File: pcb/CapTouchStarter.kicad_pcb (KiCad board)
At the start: 4 copper layers, 76.5 x 66 mm, 59 parts, among them J1 USB_C_Receptacle, J2 62684-50110, J3 Conn_ARM_JTAG_SWD_10, Q1 SS8050-G, Q2 SS8050-G, SW1 BOOT, SW2 EN, SW3 SW_SPDT, U1 CP2102N-A01-GQFN28, U2 1965-ESP32-WROOM-32E(8MB)CT-ND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

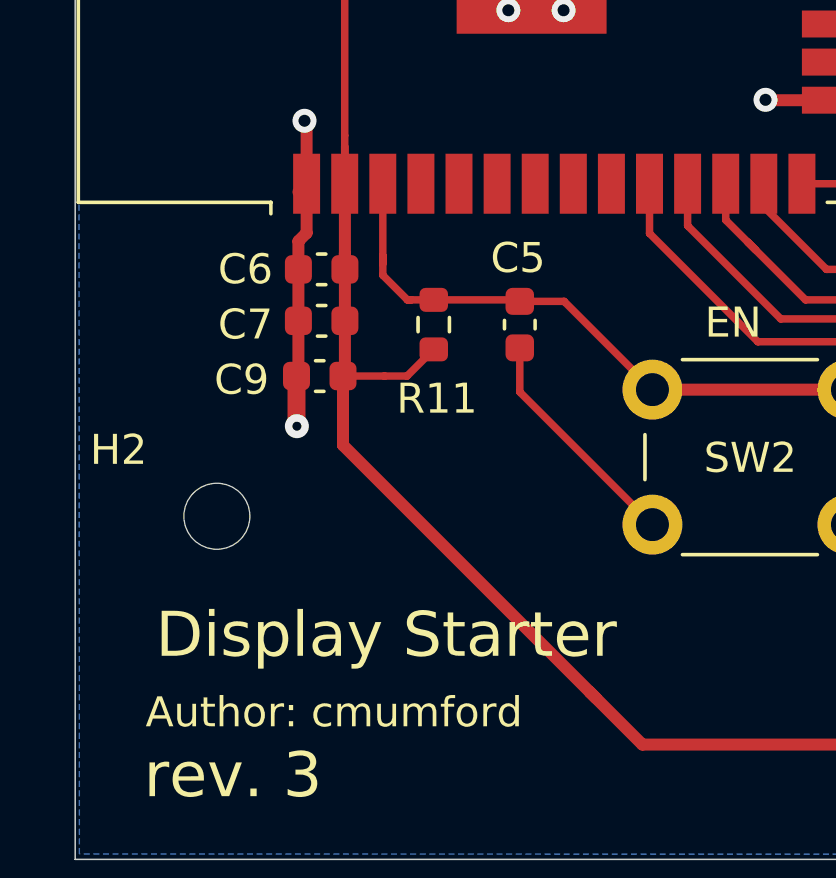
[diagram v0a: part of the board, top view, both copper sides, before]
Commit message: Add a voltage detector.
Add a BD48K33G-TLCT-ND voltage detector.
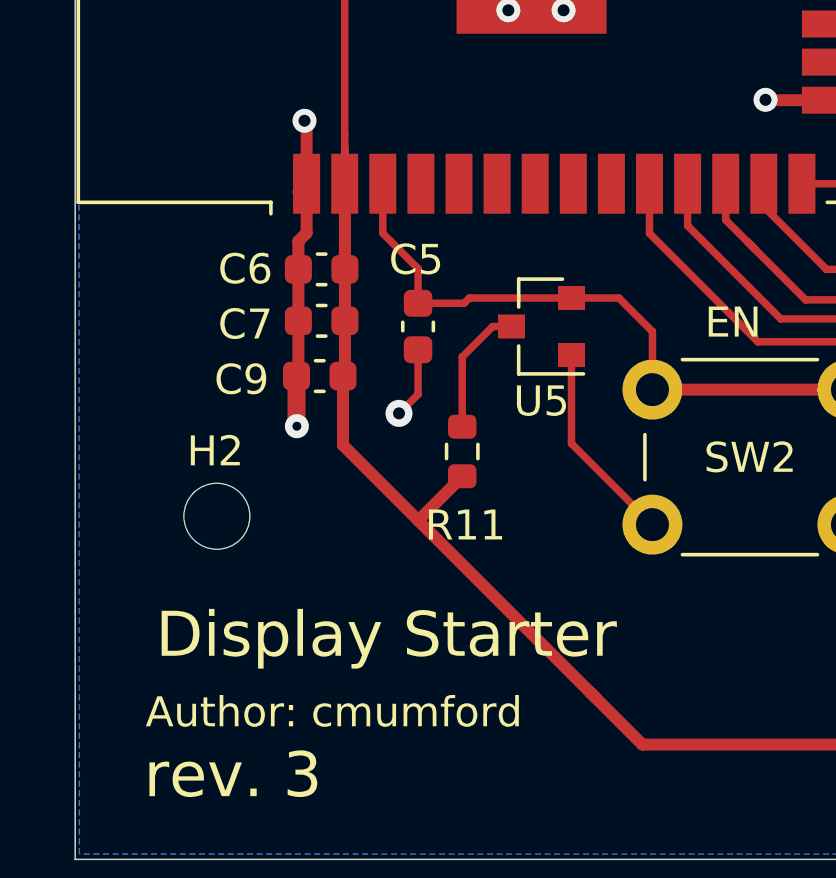
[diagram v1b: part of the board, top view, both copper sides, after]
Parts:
- added U5: BD48K33G-TLCT-ND, Package_TO_SOT_SMD:SOT-23, F.Cu at (144.0, 126.2)
- moved R11 4.33 mm to (141.4, 130.4)
- moved C5 3.39 mm to (139.9, 126.2)
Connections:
- R11 pad 2: EN -> Net-(R11-Pad2)
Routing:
- net Net-(R11-Pad2): track 0.00 -> 4.39 mm
- net GND: track 94.9 -> 96.3 mm, vias 39 -> 40
- net +3V3: track 305.0 -> 303.7 mm
- net EN: track 50.1 -> 50.9 mm

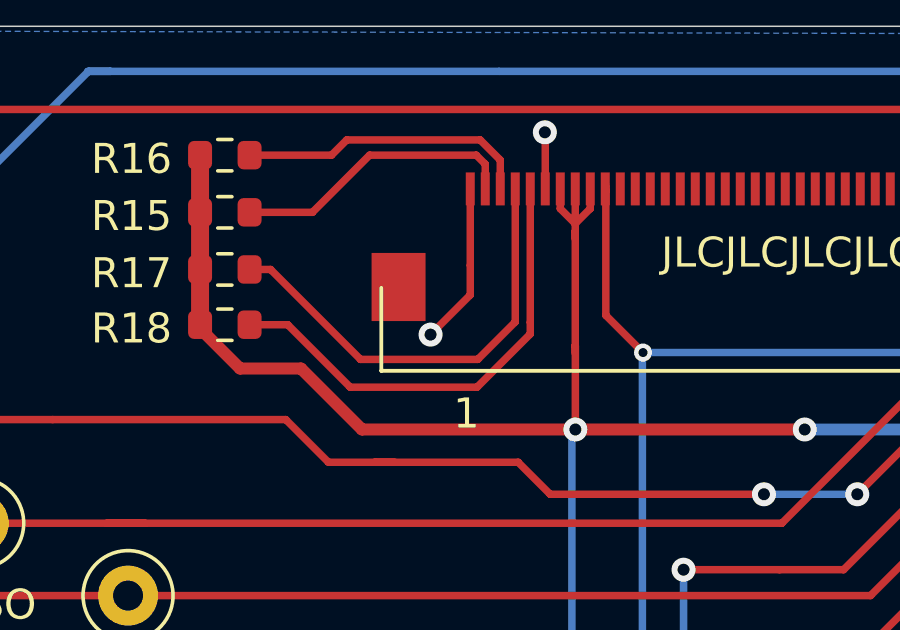
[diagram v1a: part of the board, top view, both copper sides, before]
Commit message: Fixed ground via overlapping display anchor pad.
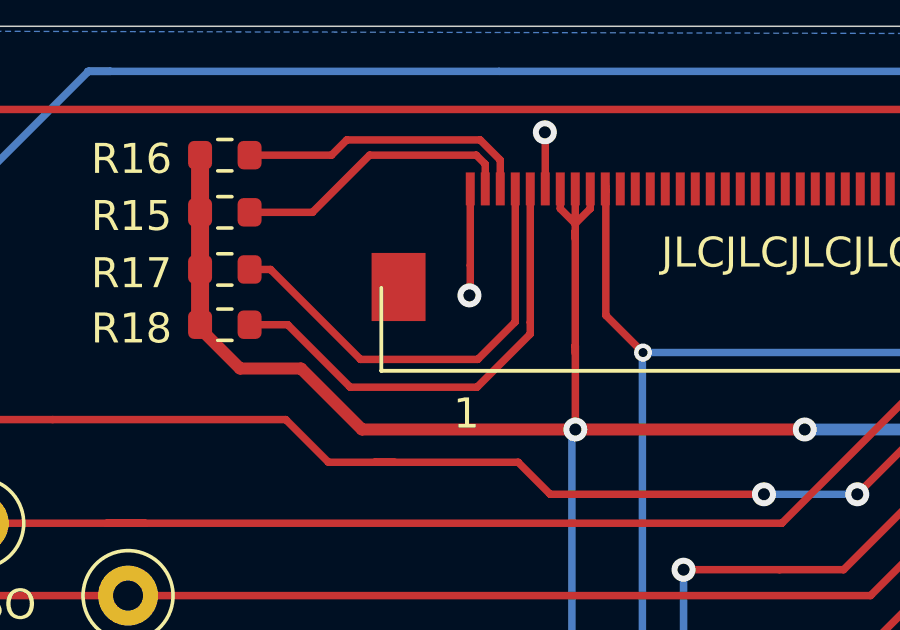
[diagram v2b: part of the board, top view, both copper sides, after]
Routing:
- net GND: track 96.3 -> 94.4 mm

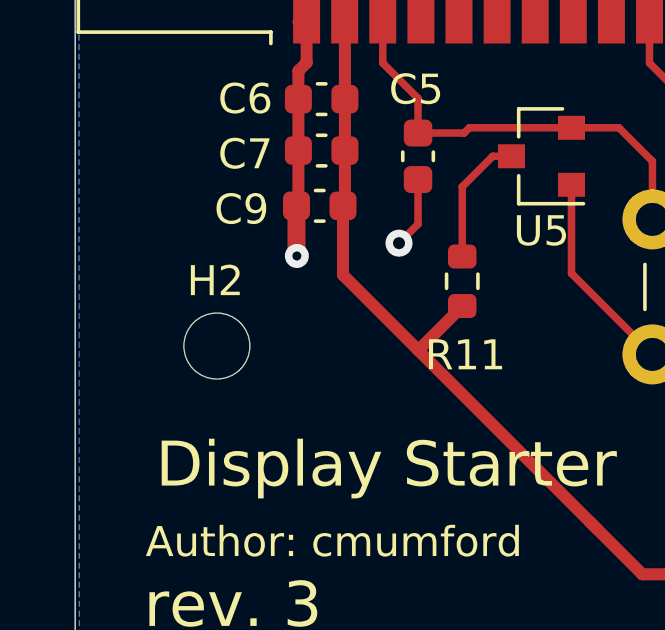
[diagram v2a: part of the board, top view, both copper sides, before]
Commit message: Added antenna keep-out zone for copper fill.
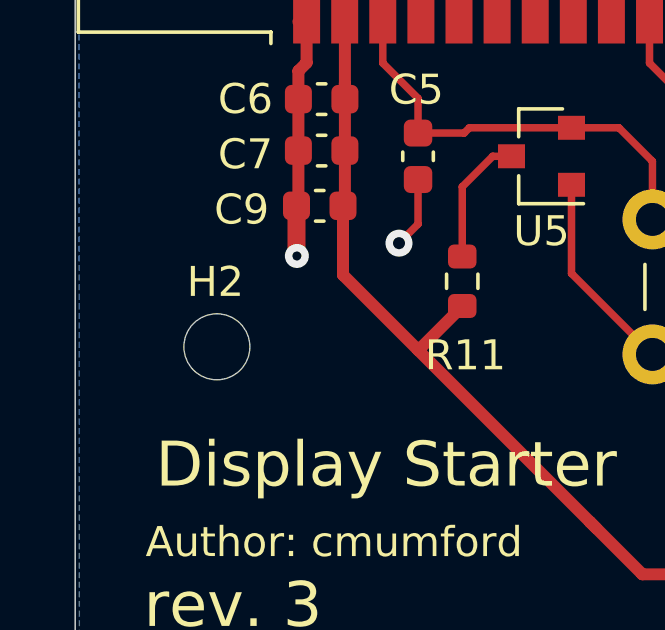
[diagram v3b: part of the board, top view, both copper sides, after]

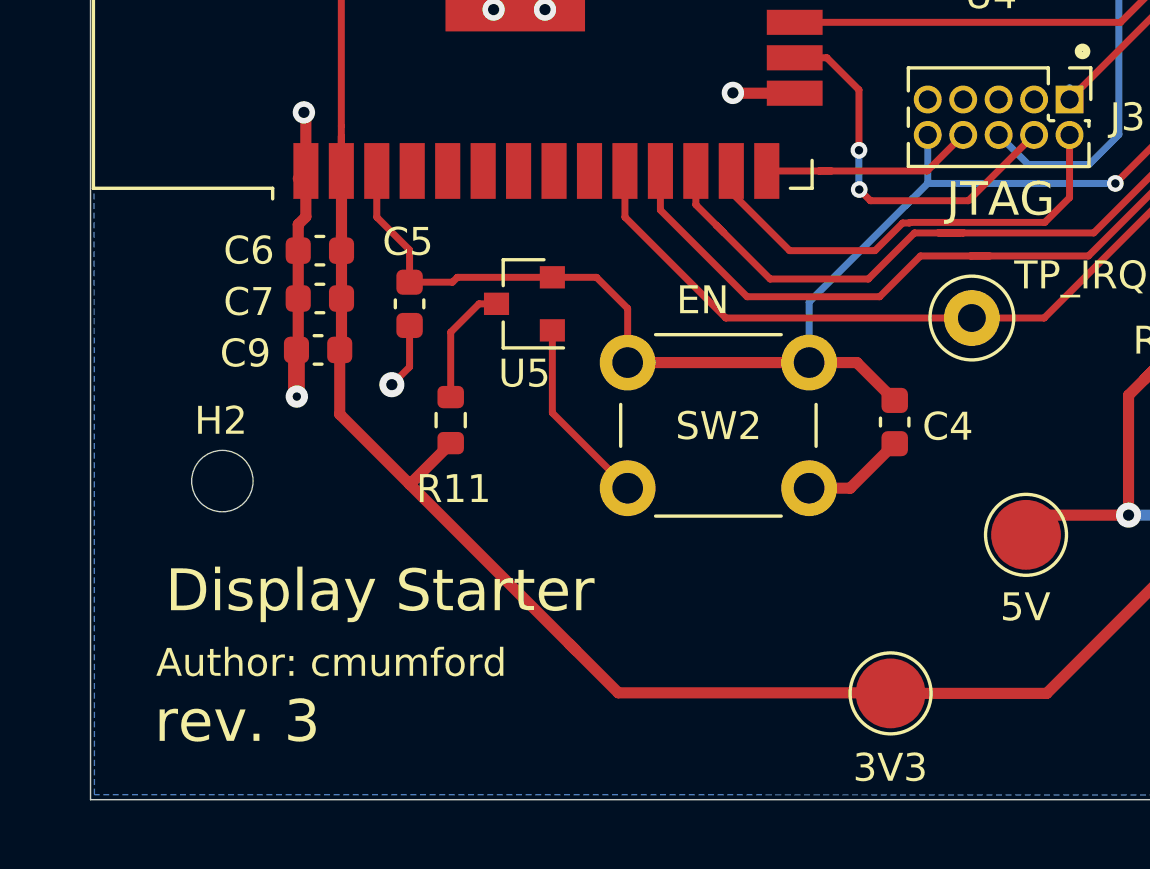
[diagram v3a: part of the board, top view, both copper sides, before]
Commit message: Added utility LED connected to IO32.
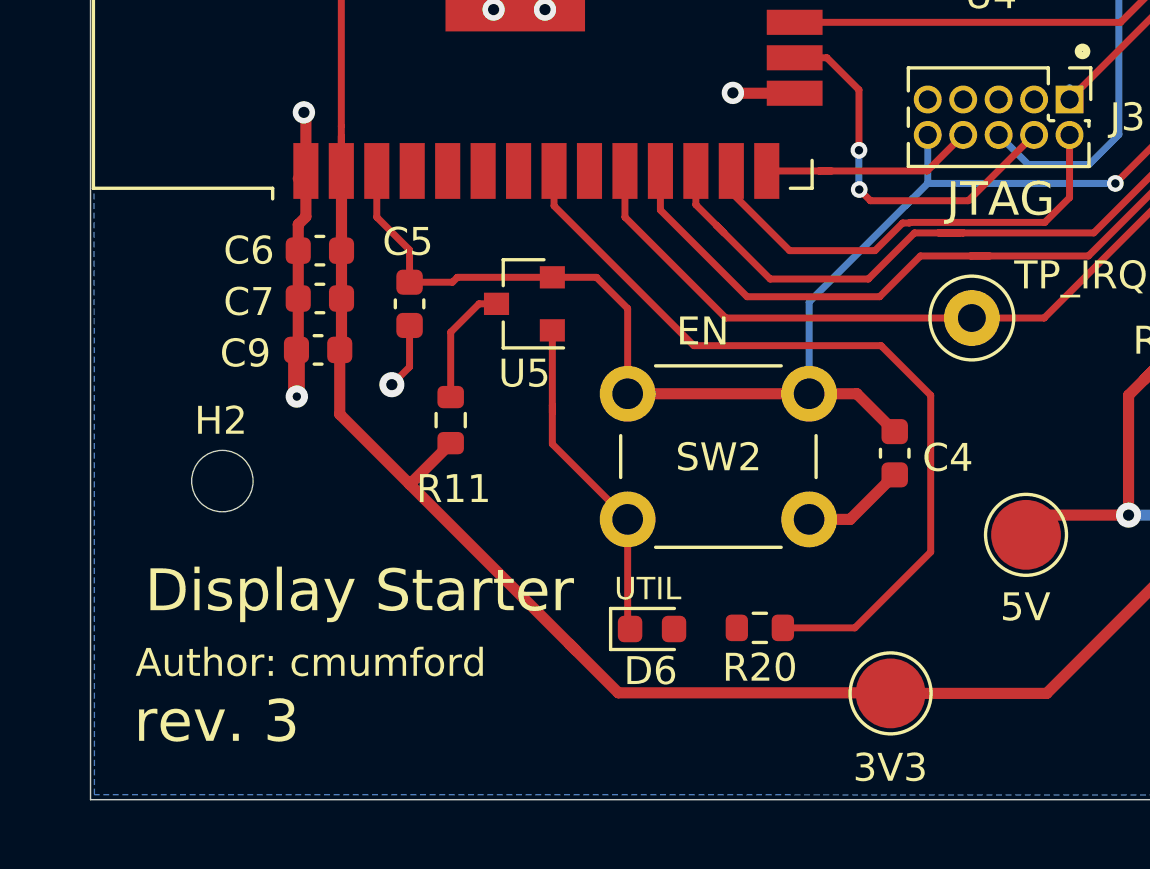
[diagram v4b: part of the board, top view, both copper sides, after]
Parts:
- added D6: UTIL, LED_SMD:LED_0603_1608Metric, F.Cu at (148.6, 137.9)
- added R20: 2KΩ, Resistor_SMD:R_0603_1608Metric, F.Cu at (152.5, 137.8)
- moved C4 1.12 mm to (157.3, 131.6)
- moved SW2 1.12 mm to (154.2, 134.0)
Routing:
- net Net-(R20-Pad1): track 0.00 -> 29.6 mm
- net GND: track 94.4 -> 99.8 mm
- net EN: track 50.9 -> 53.1 mm
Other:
- board text added: "UTIL"
